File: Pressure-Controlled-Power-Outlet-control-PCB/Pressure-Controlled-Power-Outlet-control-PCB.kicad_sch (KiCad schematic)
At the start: 47 parts, among them J1 Analog water pressure sensor 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, J2 1017514, J3 I2C0 Connector, J4 SPI1 Connector, J5 FanA 5V/24V, J6 FanB 5V/24V, K1 T9GV5L24-24, K2 T9GV5L24-24, M1 Fan_4pin, M2 Fan_4pin, Q1 2N3906, Q2 IRF540N, Q3 IRF540N, Q4 2N3906, Q5 2N3904, Q6 2N3904, Q7 2N3904, Q8 2N3904, U1 Pico, U2 LM324, U3 LF50_TO220

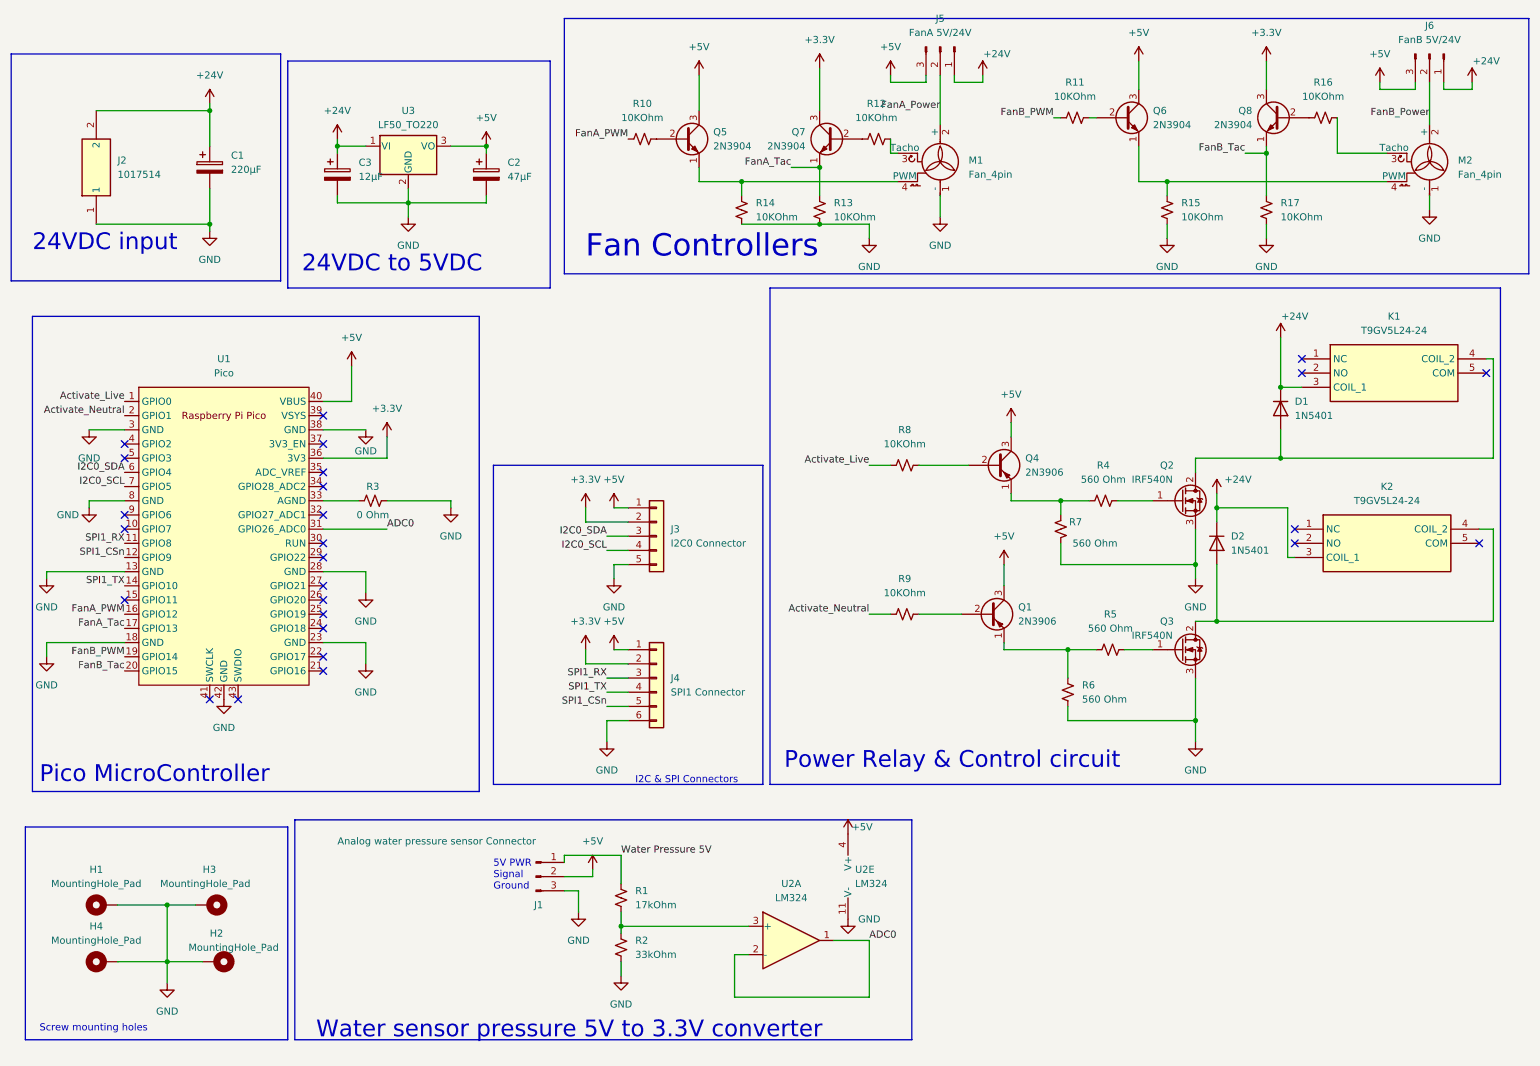
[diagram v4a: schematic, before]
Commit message: upgraded diodes to 1n5405 from 1n5401
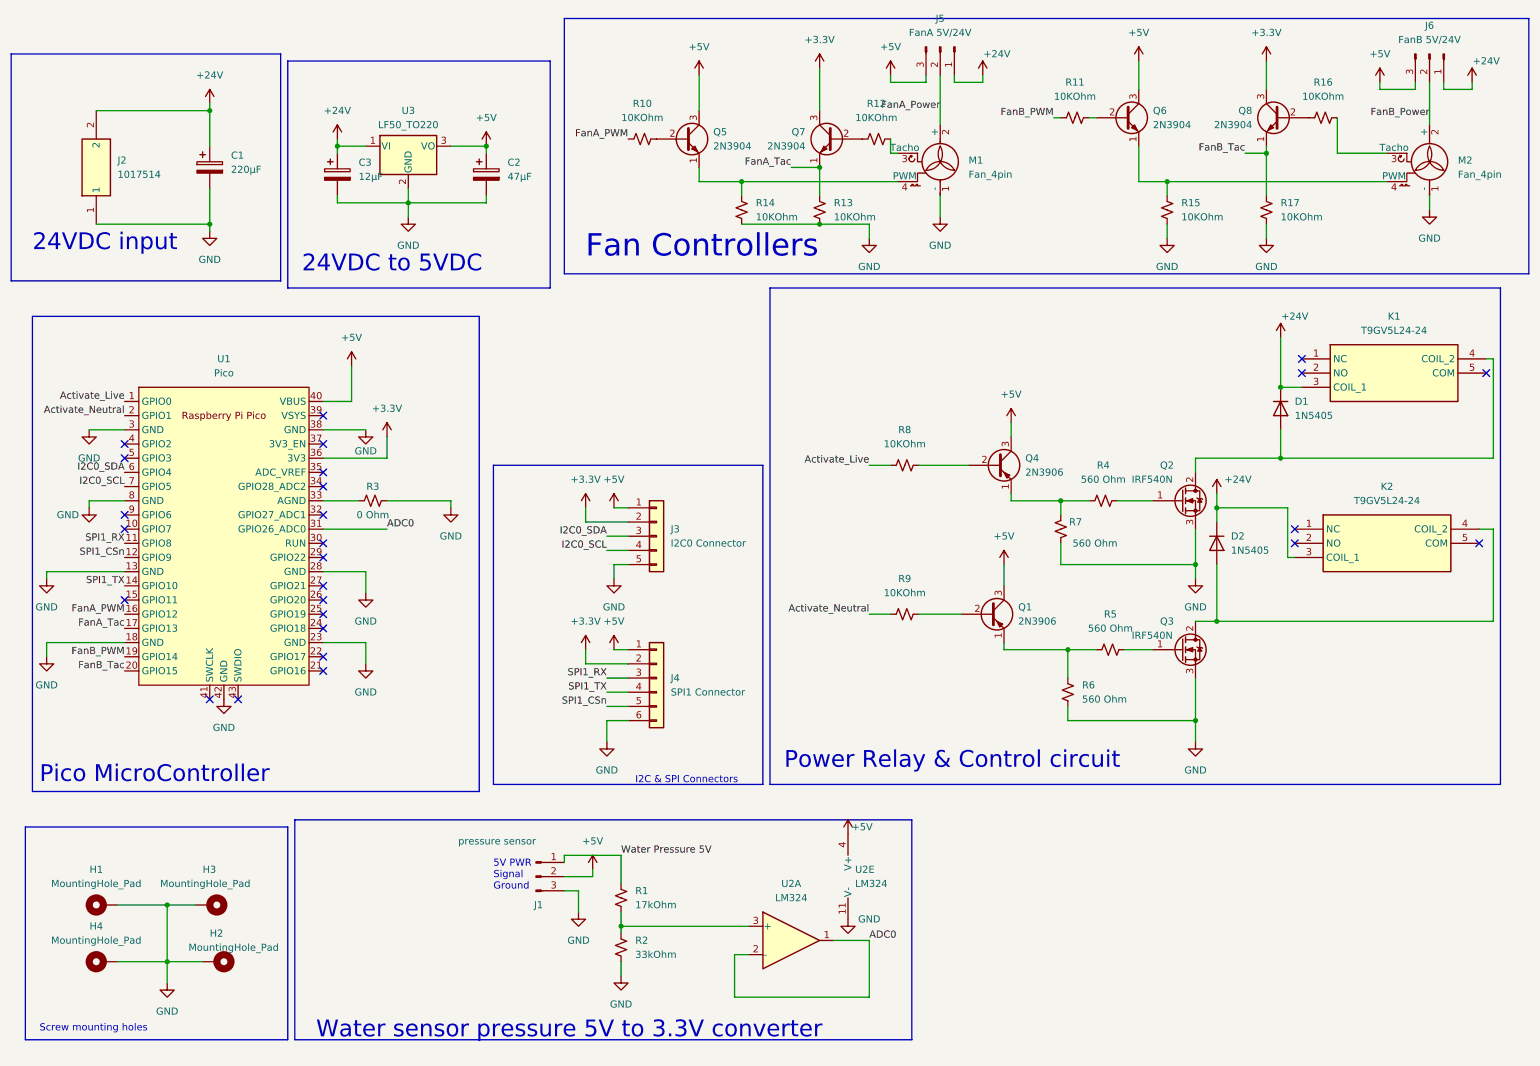
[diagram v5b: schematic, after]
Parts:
- removed D1, D2: 1N5401, Diode_THT:D_DO-201AD_P15.24mm_Horizontal, symbol Diode:1N5401
- added D1, D2: 1N5405, Diode_THT:D_DO-201AD_P15.24mm_Horizontal, symbol Diode:1N5405
- J1: value Analog water pressure sensor Connector -> pressure sensor
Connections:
- net +24V: now also D1.1 (K), D2.1 (K)
- net at K2.4 (COIL_2), Q3.2 (D): now also D2.2 (A)
- net at K1.4 (COIL_2), Q2.2 (D): now also D1.2 (A)
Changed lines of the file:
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@@
   (junction (at 201.93 125.73) (diameter 0) (color 0 0 0 0)
   )
+  (junction (at 228.6 120.65) (diameter 0) (color 0 0 0 0)
+  )
+  (junction (at 83.82 45.72) (diameter 0) (color 0 0 0 0)
+  )
+  (junction (at 157.48 49.53) (diameter 0) (color 0 0 0 0)
+  )
+  (junction (at 224.79 110.49) (diameter 0) (color 0 0 0 0)
+  )
+  (junction (at 157.48 39.37) (diameter 0) (color 0 0 0 0)
+  )
+  (junction (at 200.66 99.06) (diameter 0) (color 0 0 0 0)
+  )
+  (junction (at 48.26 49.53) (diameter 0) (color 0 0 0 0)
+  )
   (junction (at 240.03 78.74) (diameter 0) (color 0 0 0 0)
-  )
-  (junction (at 228.6 120.65) (diameter 0) (color 0 0 0 0)
-  )
-  (junction (at 83.82 45.72) (diameter 0) (color 0 0 0 0)
-  )
-  (junction (at 157.48 49.53) (diameter 0) (color 0 0 0 0)
-  )
-  (junction (at 224.79 110.49) (diameter 0) (color 0 0 0 0)
-  )
-  (junction (at 157.48 39.37) (diameter 0) (color 0 0 0 0)
-  )
-  (junction (at 200.66 99.06) (diameter 0) (color 0 0 0 0)
-  )
-  (junction (at 48.26 49.53) (diameter 0) (color 0 0 0 0)
   )
   (junction (at 71.12 35.56) (diameter 0) (color 0 0 0 0)
@@
         (path "/db34d92e-5e84-4492-8b7e-15d9a09f9218"
           (reference "U2") (unit 5)
-        )
-      )
-    )
-  )
-  (symbol (lib_id "Diode:1N5401") (at 228.6 106.68 270) (unit 1)
-    (in_bom yes) (on_board yes) (dnp no) (fields_autoplaced)
-    (property "Reference" "D2" (at 231.14 105.41 90)
-      (effects (font (size 1.27 1.27)) (justify left))
-    )
-    (property "Value" "1N5401" (at 231.14 107.95 90)
-      (effects (font (size 1.27 1.27)) (justify left))
-    )
-    (property "Footprint" "Diode_THT:D_DO-201AD_P15.24mm_Horizontal" (at 224.155 106.68 0)
-      (effects (font (size 1.27 1.27)) hide)
-    )
-    (property "Datasheet" "http://www.vishay.com/docs/88516/1n5400.pdf" (at 228.6 106.68 0)
-      (effects (font (size 1.27 1.27)) hide)
-    )
-    (property "Sim.Device" "D" (at 228.6 106.68 0)
-      (effects (font (size 1.27 1.27)) hide)
-    )
-    (property "Sim.Pins" "1=K 2=A" (at 228.6 106.68 0)
-      (effects (font (size 1.27 1.27)) hide)
-    )
-    (pin "2")
-    (pin "1")
-    (instances
-      (project "Pressure-Controlled-Power-Outlet-control-PCB"
-        (path "/db34d92e-5e84-4492-8b7e-15d9a09f9218"
-          (reference "D2") (unit 1)
         )
       )
@@
     )
   )
+  (symbol (lib_id "Diode:1N5405") (at 240.03 82.55 270) (unit 1)
+    (in_bom yes) (on_board yes) (dnp no) (fields_autoplaced)
+    (property "Reference" "D1" (at 242.57 81.28 90)
+      (effects (font (size 1.27 1.27)) (justify left))
+    )
+    (property "Value" "1N5405" (at 242.57 83.82 90)
+      (effects (font (size 1.27 1.27)) (justify left))
+    )
+    (property "Footprint" "Diode_THT:D_DO-201AD_P15.24mm_Horizontal" (at 235.585 82.55 0)
+      (effects (font (size 1.27 1.27)) hide)
+    )
+    (property "Datasheet" "http://www.vishay.com/docs/88516/1n5400.pdf" (at 240.03 82.55 0)
+      (effects (font (size 1.27 1.27)) hide)
+    )
+    (property "Sim.Device" "D" (at 240.03 82.55 0)
+      (effects (font (size 1.27 1.27)) hide)
+    )
+    (property "Sim.Pins" "1=K 2=A" (at 240.03 82.55 0)
+      (effects (font (size 1.27 1.27)) hide)
+    )
+    (pin "2")
+    (pin "1")
+    (instances
+      (project "Pressure-Controlled-Power-Outlet-control-PCB"
+        (path "/db34d92e-5e84-4492-8b7e-15d9a09f9218"
+          (reference "D1") (unit 1)
+        )
+      )
+    )
+  )
   (symbol (lib_id "Device:R_Small_US") (at 201.93 133.35 180) (unit 1)
     (in_bom yes) (on_board yes) (dnp no) (fields_autoplaced)
@@
     )
   )
-  (symbol (lib_id "Diode:1N5401") (at 240.03 82.55 270) (unit 1)
-    (in_bom yes) (on_board yes) (dnp no) (fields_autoplaced)
-    (property "Reference" "D1" (at 242.57 81.28 90)
-      (effects (font (size 1.27 1.27)) (justify left))
-    )
-    (property "Value" "1N5401" (at 242.57 83.82 90)
-      (effects (font (size 1.27 1.27)) (justify left))
-    )
-    (property "Footprint" "Diode_THT:D_DO-201AD_P15.24mm_Horizontal" (at 235.585 82.55 0)
-      (effects (font (size 1.27 1.27)) hide)
-    )
-    (property "Datasheet" "http://www.vishay.com/docs/88516/1n5400.pdf" (at 240.03 82.55 0)
-      (effects (font (size 1.27 1.27)) hide)
-    )
-    (property "Sim.Device" "D" (at 240.03 82.55 0)
-      (effects (font (size 1.27 1.27)) hide)
-    )
-    (property "Sim.Pins" "1=K 2=A" (at 240.03 82.55 0)
-      (effects (font (size 1.27 1.27)) hide)
-    )
-    (pin "2")
-    (pin "1")
-    (instances
-      (project "Pressure-Controlled-Power-Outlet-control-PCB"
-        (path "/db34d92e-5e84-4492-8b7e-15d9a09f9218"
-          (reference "D1") (unit 1)
-        )
-      )
-    )
-  )
   (symbol (lib_id "power:GND") (at 237.49 52.07 0) (unit 1)
     (in_bom yes) (on_board yes) (dnp no) (fields_autoplaced)
@@
       (effects (font (size 1.27 1.27)) (justify right))
     )
-    (property "Value" "Analog water pressure sensor Connector" (at 106.68 160.02 0)
+    (property "Value" "pressure sensor" (at 106.68 160.02 0)
       (effects (font (size 1.27 1.27)) (justify right))
     )
@@
         )
       )
+    )
+  )
+  (symbol (lib_id "Diode:1N5405") (at 228.6 106.68 270) (unit 1)
+    (in_bom yes) (on_board yes) (dnp no) (fields_autoplaced)
+    (property "Reference" "D2" (at 231.14 105.41 90)
+      (effects (font (size 1.27 1.27)) (justify left))
+    )
+    (property "Value" "1N5405" (at 231.14 107.95 90)
+      (effects (font (size 1.27 1.27)) (justify left))
+    )
+    (property "Footprint" "Diode_THT:D_DO-201AD_P15.24mm_Horizontal" (at 224.155 106.68 0)
+      (effects (font (size 1.27 1.27)) hide)
+    )
+    (property "Datasheet" "http://www.vishay.com/docs/88516/1n5400.pdf" (at 228.6 106.68 0)
+      (effects (font (size 1.27 1.27)) hide)
+    )
+    (property "Sim.Device" "D" (at 228.6 106.68 0)
+      (effects (font (size 1.27 1.27)) hide)
+    )
+    (property "Sim.Pins" "1=K 2=A" (at 228.6 106.68 0)
+      (effects (font (size 1.27 1.27)) hide)
+    )
+    (pin "2")
+    (pin "1")
+    (instances
+      (project "Pressure-Controlled-Power-Outlet-control-PCB"
+        (path "/db34d92e-5e84-4492-8b7e-15d9a09f9218"
+          (reference "D2") (unit 1)
+        )
+      )

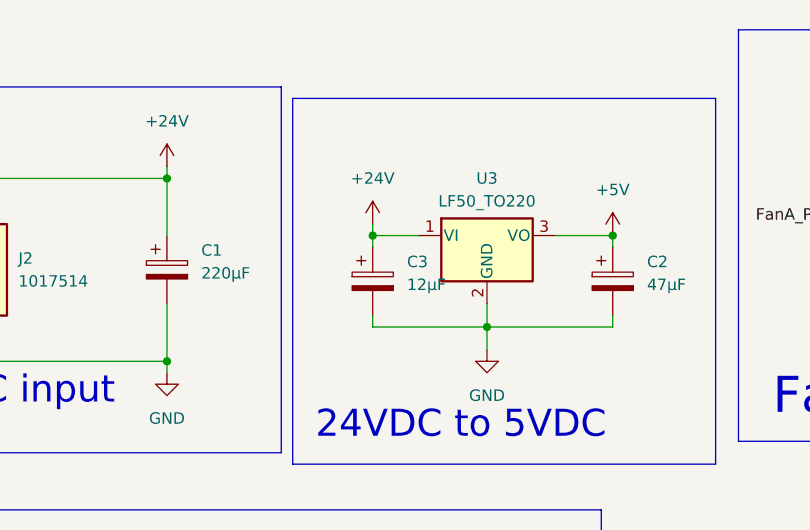
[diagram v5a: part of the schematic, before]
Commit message: added better longer lasting caps
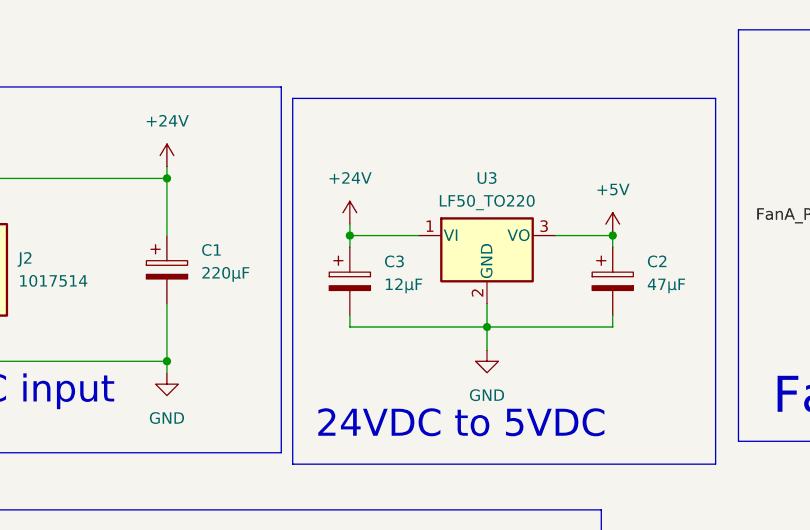
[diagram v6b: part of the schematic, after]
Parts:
- C1: footprint Capacitor_THT:CP_Radial_D8.0mm_P3.50mm -> Capacitor_THT:CP_Radial_D12.5mm_P5.00mm
- C2: footprint Capacitor_THT:CP_Radial_D5.0mm_P2.00mm -> Capacitor_THT:CP_Radial_D10.0mm_P5.00mm
- C3: footprint Capacitor_THT:CP_Radial_Tantal_D5.0mm_P2.50mm -> Capacitor_THT:CP_Radial_D10.0mm_P5.00mm
- H1, H2, H3, H4: footprint MountingHole:MountingHole_2.2mm_M2_Pad -> MountingHole:MountingHole_3.2mm_M3_DIN965_Pad
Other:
- moved on the sheet: C3
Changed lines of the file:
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@@
   (junction (at 219.71 41.91) (diameter 0) (color 0 0 0 0)
   )
+  (junction (at 68.58 35.56) (diameter 0) (color 0 0 0 0)
+  )
   (junction (at 121.92 175.26) (diameter 0) (color 0 0 0 0)
   )
@@
   )
   (junction (at 240.03 78.74) (diameter 0) (color 0 0 0 0)
-  )
-  (junction (at 71.12 35.56) (diameter 0) (color 0 0 0 0)
   )
   (junction (at 40.64 181.61) (diameter 0) (color 0 0 0 0)
@@
     (stroke (width 0) (type default))
   )
-  (wire (pts (xy 71.12 36.83) (xy 71.12 35.56))
+  (wire (pts (xy 68.58 36.83) (xy 68.58 35.56))
     (stroke (width 0) (type default))
   )
@@
     (stroke (width 0) (type default))
   )
-  (wire (pts (xy 71.12 45.72) (xy 83.82 45.72))
+  (wire (pts (xy 68.58 45.72) (xy 83.82 45.72))
     (stroke (width 0) (type default))
   )
@@
     (stroke (width 0) (type default))
   )
+  (wire (pts (xy 68.58 35.56) (xy 76.2 35.56))
+    (stroke (width 0) (type default))
+  )
   (wire (pts (xy 121.92 172.72) (xy 121.92 175.26))
     (stroke (width 0) (type default))
@@
     (stroke (width 0) (type default))
   )
-  (wire (pts (xy 71.12 35.56) (xy 76.2 35.56))
-    (stroke (width 0) (type default))
-  )
   (wire (pts (xy 224.79 91.44) (xy 224.79 93.98))
     (stroke (width 0) (type default))
@@
     (stroke (width 0) (type default))
   )
-  (wire (pts (xy 71.12 34.29) (xy 71.12 35.56))
+  (wire (pts (xy 68.58 34.29) (xy 68.58 35.56))
     (stroke (width 0) (type default))
   )
@@
     (stroke (width 0) (type default))
   )
-  (wire (pts (xy 71.12 45.72) (xy 71.12 44.45))
+  (wire (pts (xy 68.58 45.72) (xy 68.58 44.45))
     (stroke (width 0) (type default))
   )
@@
       (effects (font (size 1.27 1.27)))
     )
-    (property "Footprint" "MountingHole:MountingHole_2.2mm_M2_Pad" (at 29.21 171.45 0)
+    (property "Footprint" "MountingHole:MountingHole_3.2mm_M3_DIN965_Pad" (at 29.21 171.45 0)
       (effects (font (size 1.27 1.27)) hide)
     )
@@
       (effects (font (size 1.27 1.27)) (justify left))
     )
-    (property "Footprint" "MountingHole:MountingHole_2.2mm_M2_Pad" (at 48.26 171.45 0)
+    (property "Footprint" "MountingHole:MountingHole_3.2mm_M3_DIN965_Pad" (at 48.26 171.45 0)
       (effects (font (size 1.27 1.27)) hide)
     )
@@
     )
   )
-  (symbol (lib_id "Device:C_Polarized") (at 71.12 40.64 0) (unit 1)
-    (in_bom yes) (on_board yes) (dnp no) (fields_autoplaced)
-    (property "Reference" "C3" (at 74.93 38.481 0)
-      (effects (font (size 1.27 1.27)) (justify left))
-    )
-    (property "Value" "12µF" (at 74.93 41.021 0)
-      (effects (font (size 1.27 1.27)) (justify left))
-    )
-    (property "Footprint" "Capacitor_THT:CP_Radial_Tantal_D5.0mm_P2.50mm" (at 72.0852 44.45 0)
-      (effects (font (size 1.27 1.27)) hide)
-    )
-    (property "Datasheet" "~" (at 71.12 40.64 0)
+  (symbol (lib_id "Device:C_Polarized") (at 68.58 40.64 0) (unit 1)
+    (in_bom yes) (on_board yes) (dnp no) (fields_autoplaced)
+    (property "Reference" "C3" (at 72.39 38.481 0)
+      (effects (font (size 1.27 1.27)) (justify left))
+    )
+    (property "Value" "12µF" (at 72.39 41.021 0)
+      (effects (font (size 1.27 1.27)) (justify left))
+    )
+    (property "Footprint" "Capacitor_THT:CP_Radial_D10.0mm_P5.00mm" (at 69.5452 44.45 0)
+      (effects (font (size 1.27 1.27)) hide)
+    )
+    (property "Datasheet" "~" (at 68.58 40.64 0)
       (effects (font (size 1.27 1.27)) hide)
     )
@@
       (effects (font (size 1.27 1.27)) (justify left))
     )
-    (property "Footprint" "Capacitor_THT:CP_Radial_D5.0mm_P2.00mm" (at 98.7552 44.45 0)
+    (property "Footprint" "Capacitor_THT:CP_Radial_D10.0mm_P5.00mm" (at 98.7552 44.45 0)
       (effects (font (size 1.27 1.27)) hide)
     )
@@
       (effects (font (size 1.27 1.27)) (justify left))
     )
-    (property "Footprint" "MountingHole:MountingHole_2.2mm_M2_Pad" (at 49.53 181.61 0)
+    (property "Footprint" "MountingHole:MountingHole_3.2mm_M3_DIN965_Pad" (at 49.53 181.61 0)
       (effects (font (size 1.27 1.27)) hide)
     )
@@
     )
   )
-  (symbol (lib_id "power:+24V") (at 71.12 34.29 0) (unit 1)
-    (in_bom yes) (on_board yes) (dnp no) (fields_autoplaced)
-    (property "Reference" "#PWR015" (at 71.12 38.1 0)
-      (effects (font (size 1.27 1.27)) hide)
-    )
-    (property "Value" "+24V" (at 71.12 29.21 0)
-      (effects (font (size 1.27 1.27)))
-    )
-    (property "Footprint" "" (at 71.12 34.29 0)
-      (effects (font (size 1.27 1.27)) hide)
-    )
-    (property "Datasheet" "" (at 71.12 34.29 0)
+  (symbol (lib_id "power:+24V") (at 68.58 34.29 0) (unit 1)
+    (in_bom yes) (on_board yes) (dnp no) (fields_autoplaced)
+    (property "Reference" "#PWR015" (at 68.58 38.1 0)
+      (effects (font (size 1.27 1.27)) hide)
+    )
+    (property "Value" "+24V" (at 68.58 29.21 0)
+      (effects (font (size 1.27 1.27)))
+    )
+    (property "Footprint" "" (at 68.58 34.29 0)
+      (effects (font (size 1.27 1.27)) hide)
+    )
+    (property "Datasheet" "" (at 68.58 34.29 0)
       (effects (font (size 1.27 1.27)) hide)
     )
@@
       (effects (font (size 1.27 1.27)) (justify left))
     )
-    (property "Footprint" "Capacitor_THT:CP_Radial_D8.0mm_P3.50mm" (at 49.2252 43.18 0)
+    (property "Footprint" "Capacitor_THT:CP_Radial_D12.5mm_P5.00mm" (at 49.2252 43.18 0)
       (effects (font (size 1.27 1.27)) hide)
     )
@@
       (effects (font (size 1.27 1.27)))
     )
-    (property "Footprint" "MountingHole:MountingHole_2.2mm_M2_Pad" (at 29.21 181.61 0)
-      (effects (font (size 1.27 1.27)) hide)
-    )
+    (property "Footprint" "MountingHole:MountingHole_3.2mm_M3_DIN965_Pad" (at 29.21 181.61 0)
+      (effects (font (size 1.27 1.27)) hide)
+    )
